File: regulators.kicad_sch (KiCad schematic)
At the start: 33 parts, among them U1 MP2143DJ, U2 AP22615AWU-7, U3 LMR10510XMF

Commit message: ERC: power flags
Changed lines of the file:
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@@
   (junction (at 140.97 40.64) (diameter 0) (color 0 0 0 0)
+  )
+  (junction (at 160.655 132.08) (diameter 0) (color 0 0 0 0)
   )
   (junction (at 63.5 50.8) (diameter 0) (color 0 0 0 0)
@@
     (stroke (width 0) (type default) (color 0 0 0 0))
   )
+  (wire (pts (xy 142.24 83.82) (xy 158.75 83.82))
+    (stroke (width 0) (type default) (color 0 0 0 0))
+  )
+  (wire (pts (xy 63.5 40.64) (xy 63.5 43.18))
+    (stroke (width 0) (type default) (color 0 0 0 0))
+  )
+  (wire (pts (xy 142.24 93.98) (xy 158.75 93.98))
+    (stroke (width 0) (type default) (color 0 0 0 0))
+  )
+  (wire (pts (xy 149.86 132.08) (xy 149.86 133.35))
+    (stroke (width 0) (type default) (color 0 0 0 0))
+  )
+  (wire (pts (xy 176.53 50.8) (xy 176.53 52.07))
+    (stroke (width 0) (type default) (color 0 0 0 0))
+  )
+  (wire (pts (xy 95.25 132.08) (xy 95.25 137.16))
+    (stroke (width 0) (type default) (color 0 0 0 0))
+  )
+  (wire (pts (xy 130.81 83.82) (xy 142.24 83.82))
+    (stroke (width 0) (type default) (color 0 0 0 0))
+  )
+  (wire (pts (xy 78.74 40.64) (xy 95.25 40.64))
+    (stroke (width 0) (type default) (color 0 0 0 0))
+  )
+  (wire (pts (xy 88.9 101.6) (xy 88.9 105.41))
+    (stroke (width 0) (type default) (color 0 0 0 0))
+  )
+  (wire (pts (xy 109.22 57.15) (xy 106.68 57.15))
+    (stroke (width 0) (type default) (color 0 0 0 0))
+  )
+  (wire (pts (xy 149.86 132.08) (xy 160.655 132.08))
+    (stroke (width 0) (type default) (color 0 0 0 0))
+  )
+  (wire (pts (xy 133.35 104.14) (xy 133.35 106.68))
+    (stroke (width 0) (type default) (color 0 0 0 0))
+  )
+  (wire (pts (xy 140.97 43.18) (xy 140.97 45.72))
+    (stroke (width 0) (type default) (color 0 0 0 0))
+  )
+  (wire (pts (xy 125.73 137.16) (xy 127 137.16))
+    (stroke (width 0) (type default) (color 0 0 0 0))
+  )
+  (wire (pts (xy 95.25 132.08) (xy 110.49 132.08))
+    (stroke (width 0) (type default) (color 0 0 0 0))
+  )
+  (wire (pts (xy 124.46 179.07) (xy 124.46 182.88))
+    (stroke (width 0) (type default) (color 0 0 0 0))
+  )
+  (wire (pts (xy 134.62 132.08) (xy 137.16 132.08))
+    (stroke (width 0) (type default) (color 0 0 0 0))
+  )
+  (wire (pts (xy 95.25 40.64) (xy 95.25 41.91))
+    (stroke (width 0) (type default) (color 0 0 0 0))
+  )
+  (wire (pts (xy 88.9 93.98) (xy 88.9 96.52))
+    (stroke (width 0) (type default) (color 0 0 0 0))
+  )
+  (wire (pts (xy 95.25 40.64) (xy 109.22 40.64))
+    (stroke (width 0) (type default) (color 0 0 0 0))
+  )
+  (wire (pts (xy 63.5 83.82) (xy 63.5 85.09))
+    (stroke (width 0) (type default) (color 0 0 0 0))
+  )
+  (wire (pts (xy 78.74 40.64) (xy 78.74 43.18))
+    (stroke (width 0) (type default) (color 0 0 0 0))
+  )
+  (wire (pts (xy 176.53 40.64) (xy 176.53 41.91))
+    (stroke (width 0) (type default) (color 0 0 0 0))
+  )
+  (wire (pts (xy 158.75 81.28) (xy 158.75 83.82))
+    (stroke (width 0) (type default) (color 0 0 0 0))
+  )
+  (wire (pts (xy 46.99 80.01) (xy 46.99 83.82))
+    (stroke (width 0) (type default) (color 0 0 0 0))
+  )
+  (wire (pts (xy 158.75 40.64) (xy 158.75 41.91))
+    (stroke (width 0) (type default) (color 0 0 0 0))
+  )
+  (wire (pts (xy 115.57 179.07) (xy 115.57 182.88))
+    (stroke (width 0) (type default) (color 0 0 0 0))
+  )
   (wire (pts (xy 158.75 40.64) (xy 176.53 40.64))
     (stroke (width 0) (type default) (color 0 0 0 0))
   )
-  (wire (pts (xy 63.5 40.64) (xy 63.5 43.18))
-    (stroke (width 0) (type default) (color 0 0 0 0))
-  )
-  (wire (pts (xy 142.24 93.98) (xy 158.75 93.98))
-    (stroke (width 0) (type default) (color 0 0 0 0))
-  )
-  (wire (pts (xy 149.86 132.08) (xy 149.86 133.35))
-    (stroke (width 0) (type default) (color 0 0 0 0))
-  )
-  (wire (pts (xy 176.53 50.8) (xy 176.53 52.07))
-    (stroke (width 0) (type default) (color 0 0 0 0))
-  )
-  (wire (pts (xy 95.25 132.08) (xy 95.25 137.16))
-    (stroke (width 0) (type default) (color 0 0 0 0))
-  )
-  (wire (pts (xy 130.81 83.82) (xy 142.24 83.82))
-    (stroke (width 0) (type default) (color 0 0 0 0))
-  )
-  (wire (pts (xy 78.74 40.64) (xy 95.25 40.64))
-    (stroke (width 0) (type default) (color 0 0 0 0))
-  )
-  (wire (pts (xy 88.9 101.6) (xy 88.9 105.41))
-    (stroke (width 0) (type default) (color 0 0 0 0))
-  )
-  (wire (pts (xy 109.22 57.15) (xy 106.68 57.15))
-    (stroke (width 0) (type default) (color 0 0 0 0))
-  )
-  (wire (pts (xy 149.86 132.08) (xy 171.45 132.08))
-    (stroke (width 0) (type default) (color 0 0 0 0))
-  )
-  (wire (pts (xy 133.35 104.14) (xy 133.35 106.68))
-    (stroke (width 0) (type default) (color 0 0 0 0))
-  )
-  (wire (pts (xy 140.97 43.18) (xy 140.97 45.72))
-    (stroke (width 0) (type default) (color 0 0 0 0))
-  )
-  (wire (pts (xy 125.73 137.16) (xy 127 137.16))
-    (stroke (width 0) (type default) (color 0 0 0 0))
-  )
-  (wire (pts (xy 95.25 132.08) (xy 110.49 132.08))
-    (stroke (width 0) (type default) (color 0 0 0 0))
-  )
-  (wire (pts (xy 124.46 179.07) (xy 124.46 182.88))
-    (stroke (width 0) (type default) (color 0 0 0 0))
-  )
-  (wire (pts (xy 134.62 132.08) (xy 137.16 132.08))
-    (stroke (width 0) (type default) (color 0 0 0 0))
-  )
-  (wire (pts (xy 95.25 40.64) (xy 95.25 41.91))
-    (stroke (width 0) (type default) (color 0 0 0 0))
-  )
-  (wire (pts (xy 88.9 93.98) (xy 88.9 96.52))
-    (stroke (width 0) (type default) (color 0 0 0 0))
-  )
-  (wire (pts (xy 95.25 40.64) (xy 109.22 40.64))
-    (stroke (width 0) (type default) (color 0 0 0 0))
-  )
-  (wire (pts (xy 63.5 83.82) (xy 63.5 85.09))
-    (stroke (width 0) (type default) (color 0 0 0 0))
-  )
-  (wire (pts (xy 78.74 40.64) (xy 78.74 43.18))
-    (stroke (width 0) (type default) (color 0 0 0 0))
-  )
-  (wire (pts (xy 176.53 40.64) (xy 176.53 41.91))
-    (stroke (width 0) (type default) (color 0 0 0 0))
-  )
-  (wire (pts (xy 158.75 81.28) (xy 158.75 83.82))
-    (stroke (width 0) (type default) (color 0 0 0 0))
-  )
-  (wire (pts (xy 46.99 80.01) (xy 46.99 83.82))
-    (stroke (width 0) (type default) (color 0 0 0 0))
-  )
-  (wire (pts (xy 158.75 40.64) (xy 158.75 41.91))
-    (stroke (width 0) (type default) (color 0 0 0 0))
-  )
-  (wire (pts (xy 115.57 179.07) (xy 115.57 182.88))
-    (stroke (width 0) (type default) (color 0 0 0 0))
-  )
   (wire (pts (xy 63.5 50.8) (xy 78.74 50.8))
     (stroke (width 0) (type default) (color 0 0 0 0))
@@
     (stroke (width 0) (type default) (color 0 0 0 0))
   )
+  (wire (pts (xy 160.655 128.27) (xy 160.655 132.08))
+    (stroke (width 0) (type default) (color 0 0 0 0))
+  )
   (wire (pts (xy 134.62 132.08) (xy 134.62 133.35))
     (stroke (width 0) (type default) (color 0 0 0 0))
@@
     (stroke (width 0) (type default) (color 0 0 0 0))
   )
-  (wire (pts (xy 142.24 83.82) (xy 158.75 83.82))
-    (stroke (width 0) (type default) (color 0 0 0 0))
-  )
   (wire (pts (xy 104.14 137.16) (xy 104.14 139.7))
     (stroke (width 0) (type default) (color 0 0 0 0))
   )
+  (wire (pts (xy 160.655 132.08) (xy 171.45 132.08))
+    (stroke (width 0) (type default) (color 0 0 0 0))
+  )
   (wire (pts (xy 95.25 46.99) (xy 95.25 48.26))
     (stroke (width 0) (type default) (color 0 0 0 0))
@@
     (stroke (width 0) (type default) (color 0 0 0 0))
   )
-  (text "I_{max} = 1A" (at 149.86 130.81 0)
+  (text "I_{max} = 1A" (at 144.145 130.81 0)
     (effects (font (size 1.9 1.9)) (justify left bottom))
   )
@@
     (pin "2")
   )
+  (symbol (lib_id "power:PWR_FLAG") (at 160.655 128.27 0) (unit 1)
+    (in_bom yes) (on_board yes) (fields_autoplaced)
+    (property "Reference" "#FLG04" (id 0) (at 160.655 126.365 0)
+      (effects (font (size 1.27 1.27)) hide)
+    )
+    (property "Value" "PWR_FLAG" (id 1) (at 160.655 123.19 0))
+    (property "Footprint" "" (id 2) (at 160.655 128.27 0)
+      (effects (font (size 1.27 1.27)) hide)
+    )
+    (property "Datasheet" "~" (id 3) (at 160.655 128.27 0)
+      (effects (font (size 1.27 1.27)) hide)
+    )
+    (pin "1")
+  )
   (symbol (lib_id "power:GND") (at 105.41 100.33 0) (unit 1)

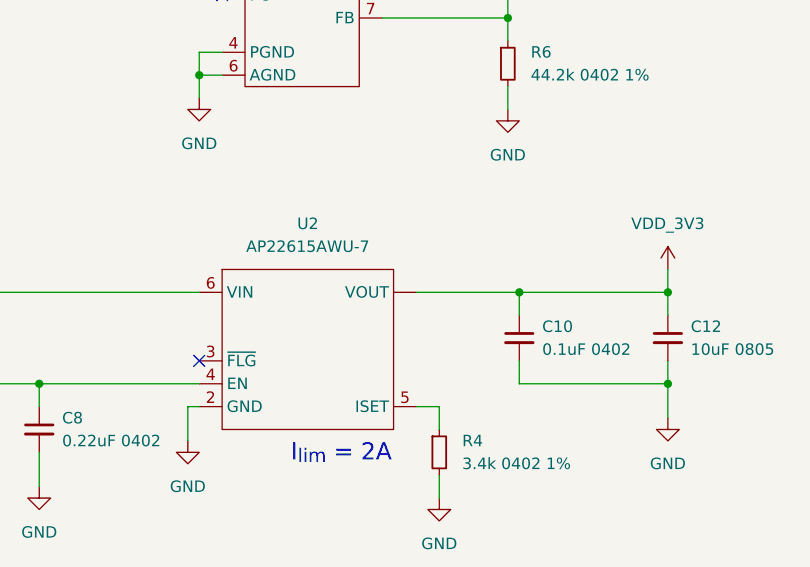
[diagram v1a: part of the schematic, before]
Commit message: Update symbols
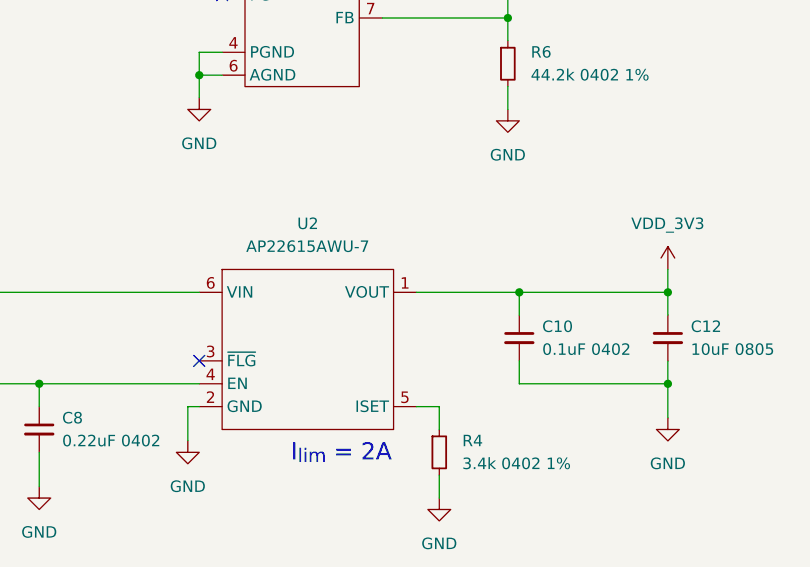
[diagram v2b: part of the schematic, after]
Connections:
- net VDD_3V3: now also U2.1 (VOUT); no longer U2. (VOUT)
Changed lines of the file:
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@@
       (effects (font (size 1.27 1.27)) hide)
     )
-    (pin "")
+    (pin "1")
     (pin "2")
     (pin "3")

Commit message: Footprint assignments for standard passives
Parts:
- C1, C11, C12, C13, C2, C3, C5, C7: footprint (none) -> Capacitor_SMD:C_0805_2012Metric
- C10, C14, C4, C6, C8, C9: footprint (none) -> Capacitor_SMD:C_0402_1005Metric
- R1, R2, R3, R4, R6, R7, R8: footprint (none) -> Resistor_SMD:R_0402_1005Metric
- R5: footprint (none) -> Resistor_SMD:R_0603_1608Metric
- TP1, TP2, TP3, TP4, TP5: footprint (none) -> TestPoint:TestPoint_Pad_D1.5mm
- U3: footprint Package_TO_SOT_SMD:SOT-23-5 -> (none)
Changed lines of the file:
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@@
       (effects (font (size 1.27 1.27)) (justify left))
     )
-    (property "Footprint" "" (id 2) (at 140.97 58.42 0)
+    (property "Footprint" "Resistor_SMD:R_0402_1005Metric" (id 2) (at 140.97 58.42 0)
       (effects (font (size 1.27 1.27)) hide)
     )
@@
       (effects (font (size 1.27 1.27)) (justify left))
     )
-    (property "Footprint" "" (id 2) (at 176.53 44.45 0)
+    (property "Footprint" "Capacitor_SMD:C_0402_1005Metric" (id 2) (at 176.53 44.45 0)
       (effects (font (size 1.27 1.27)) hide)
     )
@@
       (effects (font (size 1.27 1.27)) (justify right) hide)
     )
-    (property "Footprint" "" (id 2) (at 90.17 182.88 0)
+    (property "Footprint" "TestPoint:TestPoint_Pad_D1.5mm" (id 2) (at 90.17 182.88 0)
       (effects (font (size 1.27 1.27)) hide)
     )
@@
       (effects (font (size 1.27 1.27)) (justify left))
     )
-    (property "Footprint" "" (id 2) (at 140.97 48.26 0)
+    (property "Footprint" "Resistor_SMD:R_0603_1608Metric" (id 2) (at 140.97 48.26 0)
       (effects (font (size 1.27 1.27)) hide)
     )
@@
       (effects (font (size 1.27 1.27)) (justify left))
     )
-    (property "Footprint" "" (id 2) (at 46.99 87.63 0)
+    (property "Footprint" "Capacitor_SMD:C_0805_2012Metric" (id 2) (at 46.99 87.63 0)
       (effects (font (size 1.27 1.27)) hide)
     )
@@
       (effects (font (size 1.27 1.27)) (justify left))
     )
-    (property "Footprint" "" (id 2) (at 78.74 135.89 0)
+    (property "Footprint" "Capacitor_SMD:C_0805_2012Metric" (id 2) (at 78.74 135.89 0)
       (effects (font (size 1.27 1.27)) hide)
     )
@@
       (effects (font (size 1.27 1.27)) (justify left))
     )
-    (property "Footprint" "" (id 2) (at 158.75 88.9 0)
+    (property "Footprint" "Capacitor_SMD:C_0805_2012Metric" (id 2) (at 158.75 88.9 0)
       (effects (font (size 1.27 1.27)) hide)
     )
@@
       (effects (font (size 1.27 1.27)) (justify left))
     )
-    (property "Footprint" "" (id 2) (at 48.26 45.72 0)
+    (property "Footprint" "Capacitor_SMD:C_0805_2012Metric" (id 2) (at 48.26 45.72 0)
       (effects (font (size 1.27 1.27)) hide)
     )
@@
     (property "Reference" "R1" (id 0) (at 80.01 91.44 90))
     (property "Value" "100k 0402" (id 1) (at 80.01 96.52 90))
-    (property "Footprint" "" (id 2) (at 80.01 93.98 0)
+    (property "Footprint" "Resistor_SMD:R_0402_1005Metric" (id 2) (at 80.01 93.98 0)
       (effects (font (size 1.27 1.27)) hide)
     )
@@
       (effects (font (size 1.27 1.27)) (justify left))
     )
-    (property "Footprint" "" (id 2) (at 63.5 87.63 0)
+    (property "Footprint" "Capacitor_SMD:C_0402_1005Metric" (id 2) (at 63.5 87.63 0)
       (effects (font (size 1.27 1.27)) hide)
     )
@@
     (property "Reference" "U3" (id 0) (at 118.11 124.46 0))
     (property "Value" "LMR10510XMF" (id 1) (at 118.11 127 0))
-    (property "Footprint" "Package_TO_SOT_SMD:SOT-23-5" (id 2) (at 119.38 140.97 0)
+    (property "Footprint" "" (id 2) (at 119.38 140.97 0)
       (effects (font (size 1.27 1.27) italic) (justify left) hide)
     )
@@
       (effects (font (size 1.27 1.27)) (justify left))
     )
-    (property "Footprint" "" (id 2) (at 63.5 45.72 0)
+    (property "Footprint" "Capacitor_SMD:C_0805_2012Metric" (id 2) (at 63.5 45.72 0)
       (effects (font (size 1.27 1.27)) hide)
     )
@@
       (effects (font (size 1.27 1.27)) (justify right) hide)
     )
-    (property "Footprint" "" (id 2) (at 110.49 182.88 0)
+    (property "Footprint" "TestPoint:TestPoint_Pad_D1.5mm" (id 2) (at 110.49 182.88 0)
       (effects (font (size 1.27 1.27)) hide)
     )
@@
       (effects (font (size 1.27 1.27)) (justify left))
     )
-    (property "Footprint" "" (id 2) (at 149.86 153.67 0)
+    (property "Footprint" "Resistor_SMD:R_0402_1005Metric" (id 2) (at 149.86 153.67 0)
       (effects (font (size 1.27 1.27)) hide)
     )
@@
       (effects (font (size 1.27 1.27)) (justify left))
     )
-    (property "Footprint" "" (id 2) (at 104.14 142.24 0)
+    (property "Footprint" "Capacitor_SMD:C_0402_1005Metric" (id 2) (at 104.14 142.24 0)
       (effects (font (size 1.27 1.27)) hide)
     )
@@
       (effects (font (size 1.27 1.27)) (justify left))
     )
-    (property "Footprint" "" (id 2) (at 149.86 135.89 0)
+    (property "Footprint" "Resistor_SMD:R_0402_1005Metric" (id 2) (at 149.86 135.89 0)
       (effects (font (size 1.27 1.27)) hide)
     )
@@
       (effects (font (size 1.27 1.27)) (justify left))
     )
-    (property "Footprint" "" (id 2) (at 78.74 45.72 0)
+    (property "Footprint" "Capacitor_SMD:C_0402_1005Metric" (id 2) (at 78.74 45.72 0)
       (effects (font (size 1.27 1.27)) hide)
     )
@@
     (property "Reference" "R3" (id 0) (at 97.79 134.62 90))
     (property "Value" "10k 0402" (id 1) (at 97.79 139.7 90))
-    (property "Footprint" "" (id 2) (at 97.79 137.16 0)
+    (property "Footprint" "Resistor_SMD:R_0402_1005Metric" (id 2) (at 97.79 137.16 0)
       (effects (font (size 1.27 1.27)) hide)
     )
@@
       (effects (font (size 1.27 1.27)) (justify left))
     )
-    (property "Footprint" "" (id 2) (at 88.9 99.06 0)
+    (property "Footprint" "Capacitor_SMD:C_0402_1005Metric" (id 2) (at 88.9 99.06 0)
       (effects (font (size 1.27 1.27)) hide)
     )
@@
       (effects (font (size 1.27 1.27)) (justify left))
     )
-    (property "Footprint" "" (id 2) (at 158.75 44.45 0)
+    (property "Footprint" "Capacitor_SMD:C_0805_2012Metric" (id 2) (at 158.75 44.45 0)
       (effects (font (size 1.27 1.27)) hide)
     )
@@
       (effects (font (size 1.27 1.27)) (justify right) hide)
     )
-    (property "Footprint" "" (id 2) (at 119.38 182.88 0)
+    (property "Footprint" "TestPoint:TestPoint_Pad_D1.5mm" (id 2) (at 119.38 182.88 0)
       (effects (font (size 1.27 1.27)) hide)
     )
@@
       (effects (font (size 1.27 1.27)) (justify left))
     )
-    (property "Footprint" "" (id 2) (at 171.45 137.16 0)
+    (property "Footprint" "Capacitor_SMD:C_0805_2012Metric" (id 2) (at 171.45 137.16 0)
       (effects (font (size 1.27 1.27)) hide)
     )
@@
       (effects (font (size 1.27 1.27)) (justify left))
     )
-    (property "Footprint" "" (id 2) (at 63.5 135.89 0)
+    (property "Footprint" "Capacitor_SMD:C_0805_2012Metric" (id 2) (at 63.5 135.89 0)
       (effects (font (size 1.27 1.27)) hide)
     )
@@
       (effects (font (size 1.27 1.27)) (justify left))
     )
-    (property "Footprint" "" (id 2) (at 138.43 179.07 0)
+    (property "Footprint" "TestPoint:TestPoint_Pad_D1.5mm" (id 2) (at 138.43 179.07 0)
       (effects (font (size 1.27 1.27)) hide)
     )
@@
       (effects (font (size 1.27 1.27)) (justify left))
     )
-    (property "Footprint" "" (id 2) (at 95.25 44.45 0)
+    (property "Footprint" "Resistor_SMD:R_0402_1005Metric" (id 2) (at 95.25 44.45 0)
       (effects (font (size 1.27 1.27)) hide)
     )
@@
       (effects (font (size 1.27 1.27)) (justify left))
     )
-    (property "Footprint" "" (id 2) (at 133.35 101.6 0)
+    (property "Footprint" "Resistor_SMD:R_0402_1005Metric" (id 2) (at 133.35 101.6 0)
       (effects (font (size 1.27 1.27)) hide)
     )
@@
       (effects (font (size 1.27 1.27)) (justify left))
     )
-    (property "Footprint" "" (id 2) (at 142.24 88.9 0)
+    (property "Footprint" "Capacitor_SMD:C_0402_1005Metric" (id 2) (at 142.24 88.9 0)
       (effects (font (size 1.27 1.27)) hide)
     )
@@
       (effects (font (size 1.27 1.27)) (justify right) hide)
     )
-    (property "Footprint" "" (id 2) (at 100.33 182.88 0)
-      (effects (font (size 1.27 1.27)) hide)
-    )
+    (property "Footprint" "TestPoint:TestPoint_Pad_D1.5mm" (id 2) (at 100.33 182.88 0)
+      (effects (font (size 1.27 1.27)) hide)
+    )
